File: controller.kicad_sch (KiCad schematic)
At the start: 42 parts, among them J10 Btn 3, J11 GND, J3 JTAG, J4 DM3AT-SF-PEJM5, J5 Volume, J6 Btn 0, J7 RS485, J8 Btn 1, J9 Btn 2, SW1 Reset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

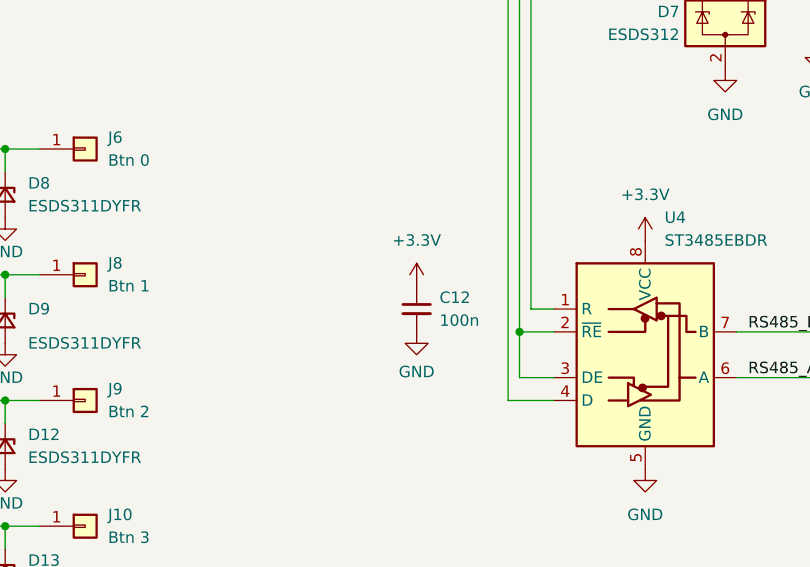
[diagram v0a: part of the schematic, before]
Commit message: Changed some labes, fixed RS485 Line Fixed Servo-Pin Header and Audio-Pin Header label. Added 10k Pullup to RS485 R-Line
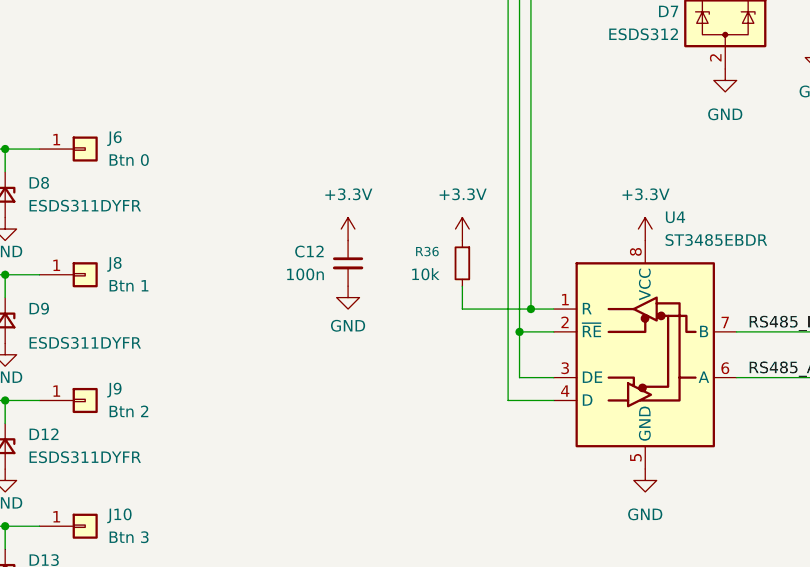
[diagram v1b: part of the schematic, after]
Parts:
- added R36: 10k, Resistor_SMD:R_0603_1608Metric, symbol Device:R_Small
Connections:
- net +3.3V: now also R36.1
- net RS485_R: now also R36.2
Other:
- moved on the sheet: C12
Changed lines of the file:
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@@
 	)
 	(junction
+		(at 110.49 147.32)
+		(diameter 0)
+		(color 0 0 0 0)
+	)
+	(junction
 		(at 191.77 68.58)
 		(diameter 0)
@@
 	(wire
 		(pts
+			(xy 102.87 147.32) (xy 110.49 147.32)
+		)
+		(stroke
+			(width 0)
+			(type default)
+		)
+	)
+	(wire
+		(pts
 			(xy 208.28 66.04) (xy 229.87 66.04)
 		)
@@
 	(wire
 		(pts
+			(xy 102.87 144.78) (xy 102.87 147.32)
+		)
+		(stroke
+			(width 0)
+			(type default)
+		)
+	)
+	(wire
+		(pts
 			(xy 91.44 88.9) (xy 114.3 88.9)
 		)
@@
 	(symbol
 		(lib_id "power:+3.3V")
-		(at 97.79 144.78 0)
+		(at 102.87 139.7 0)
+		(unit 1)
+		(exclude_from_sim no)
+		(in_bom yes)
+		(on_board yes)
+		(dnp no)
+		(fields_autoplaced yes)
+		(property "Reference" "#PWR058"
+			(at 102.87 143.51 0)
+			(effects
+				(font
+					(size 1.27 1.27)
+				)
+				(hide yes)
+			)
+		)
+		(property "Value" "+3.3V"
+			(at 102.87 134.62 0)
+			(effects
+				(font
+					(size 1.27 1.27)
+				)
+			)
+		)
+		(property "Footprint" ""
+			(at 102.87 139.7 0)
+			(effects
+				(font
+					(size 1.27 1.27)
+				)
+				(hide yes)
+			)
+		)
+		(property "Datasheet" ""
+			(at 102.87 139.7 0)
+			(effects
+				(font
+					(size 1.27 1.27)
+				)
+				(hide yes)
+			)
+		)
+		(property "Description" "Power symbol creates a global label with name \"+3.3V\""
+			(at 102.87 139.7 0)
+			(effects
+				(font
+					(size 1.27 1.27)
+				)
+				(hide yes)
+			)
+		)
+		(pin "1"
+		)
+		(instances
+			(project "BigCore"
+				(path "/9351c569-8a22-403a-823f-92ee14b5d151/f9df186a-d40d-4358-a69d-aed97d34e621"
+					(reference "#PWR058")
+					(unit 1)
+				)
+			)
+		)
+	)
+	(symbol
+		(lib_id "power:+3.3V")
+		(at 90.17 139.7 0)
 		(unit 1)
 		(exclude_from_sim no)
@@
 		(fields_autoplaced yes)
 		(property "Reference" "#PWR053"
-			(at 97.79 148.59 0)
+			(at 90.17 143.51 0)
 			(effects
 				(font
@@
 		)
 		(property "Value" "+3.3V"
-			(at 97.79 139.7 0)
+			(at 90.17 134.62 0)
 			(effects
 				(font
@@
 		)
 		(property "Footprint" ""
-			(at 97.79 144.78 0)
+			(at 90.17 139.7 0)
 			(effects
 				(font
@@
 		)
 		(property "Datasheet" ""
-			(at 97.79 144.78 0)
+			(at 90.17 139.7 0)
 			(effects
 				(font
@@
 		)
 		(property "Description" "Power symbol creates a global label with name \"+3.3V\""
-			(at 97.79 144.78 0)
+			(at 90.17 139.7 0)
 			(effects
 				(font
@@
 	)
 	(symbol
+		(lib_id "Device:R_Small")
+		(at 102.87 142.24 0)
+		(mirror y)
+		(unit 1)
+		(exclude_from_sim no)
+		(in_bom yes)
+		(on_board yes)
+		(dnp no)
+		(property "Reference" "R36"
+			(at 100.33 140.9699 0)
+			(effects
+				(font
+					(size 1.016 1.016)
+				)
+				(justify left)
+			)
+		)
+		(property "Value" "10k"
+			(at 100.33 143.5099 0)
+			(effects
+				(font
+					(size 1.27 1.27)
+				)
+				(justify left)
+			)
+		)
+		(property "Footprint" "Resistor_SMD:R_0603_1608Metric"
+			(at 102.87 142.24 0)
+			(effects
+				(font
+					(size 1.27 1.27)
+				)
+				(hide yes)
+			)
+		)
+		(property "Datasheet" "~"
+			(at 102.87 142.24 0)
+			(effects
+				(font
+					(size 1.27 1.27)
+				)
+				(hide yes)
+			)
+		)
+		(property "Description" "Resistor, small symbol"
+			(at 102.87 142.24 0)
+			(effects
+				(font
+					(size 1.27 1.27)
+				)
+				(hide yes)
+			)
+		)
+		(pin "2"
+		)
+		(pin "1"
+		)
+		(instances
+			(project "BigCore"
+				(path "/9351c569-8a22-403a-823f-92ee14b5d151/f9df186a-d40d-4358-a69d-aed97d34e621"
+					(reference "R36")
+					(unit 1)
+				)
+			)
+		)
+	)
+	(symbol
 		(lib_id "Connector_Generic:Conn_01x01")
 		(at 60.96 185.42 0)
@@
 	(symbol
 		(lib_id "Device:C_Small")
-		(at 97.79 147.32 0)
+		(at 90.17 142.24 0)
+		(mirror y)
 		(unit 1)
 		(exclude_from_sim no)
@@
 		(dnp no)
 		(property "Reference" "C12"
-			(at 100.33 146.0562 0)
+			(at 87.63 140.9762 0)
 			(effects
 				(font
@@
 		)
 		(property "Value" "100n"
-			(at 100.33 148.5962 0)
+			(at 87.63 143.5162 0)
 			(effects
 				(font
@@
 		)
 		(property "Footprint" "Capacitor_SMD:C_0603_1608Metric"
-			(at 97.79 147.32 0)
+			(at 90.17 142.24 0)
 			(effects
 				(font
@@
 		)
 		(property "Datasheet" "~"
-			(at 97.79 147.32 0)
+			(at 90.17 142.24 0)
 			(effects
 				(font
@@
 		)
 		(property "Description" "Unpolarized capacitor, small symbol"
-			(at 97.79 147.32 0)
+			(at 90.17 142.24 0)
 			(effects
 				(font
@@
 	(symbol
 		(lib_id "power:GND")
-		(at 97.79 149.86 0)
+		(at 90.17 144.78 0)
 		(unit 1)
 		(exclude_from_sim no)
@@
 		(dnp no)
 		(property "Reference" "#PWR054"
-			(at 97.79 156.21 0)
+			(at 90.17 151.13 0)
 			(effects
 				(font
@@
 		)
 		(property "Value" "GND"
-			(at 97.79 154.305 0)
+			(at 90.17 149.225 0)
 			(effects
 				(font
@@
 		)
 		(property "Footprint" ""
-			(at 97.79 149.86 0)
+			(at 90.17 144.78 0)
 			(effects
 				(font
@@
 		)
 		(property "Datasheet" ""
-			(at 97.79 149.86 0)
+			(at 90.17 144.78 0)
 			(effects
 				(font
@@
 		)
 		(property "Description" "Power symbol creates a global label with name \"GND\" , ground"
-			(at 97.79 149.86 0)
+			(at 90.17 144.78 0)
 			(effects
 				(font
